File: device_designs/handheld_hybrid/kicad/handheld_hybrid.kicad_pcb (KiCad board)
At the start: 4 copper layers, 220 x 110 mm, 6 parts

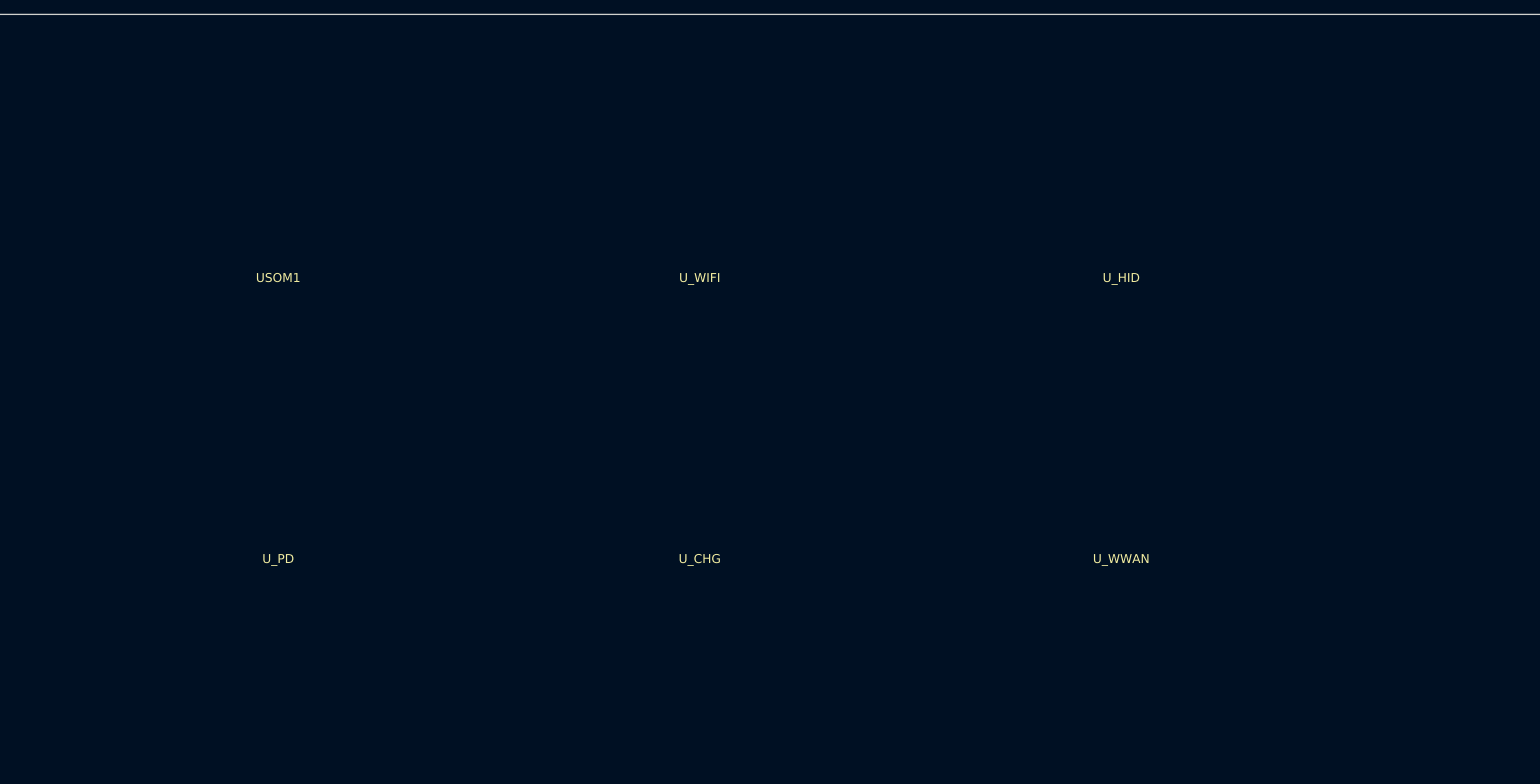
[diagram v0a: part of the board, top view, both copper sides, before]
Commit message: feat(eda): Cont VII release-clean ledger + ERC/DRC zero-error revalidation
Investigate every Cont VI ERC/DRC entry, wire functional nets, clear error-class
violations, and publish honest release-clean tokens (CLI pass ≠ clean pass).

Co-authored-by: Cursor <cursoragent@cursor.com>
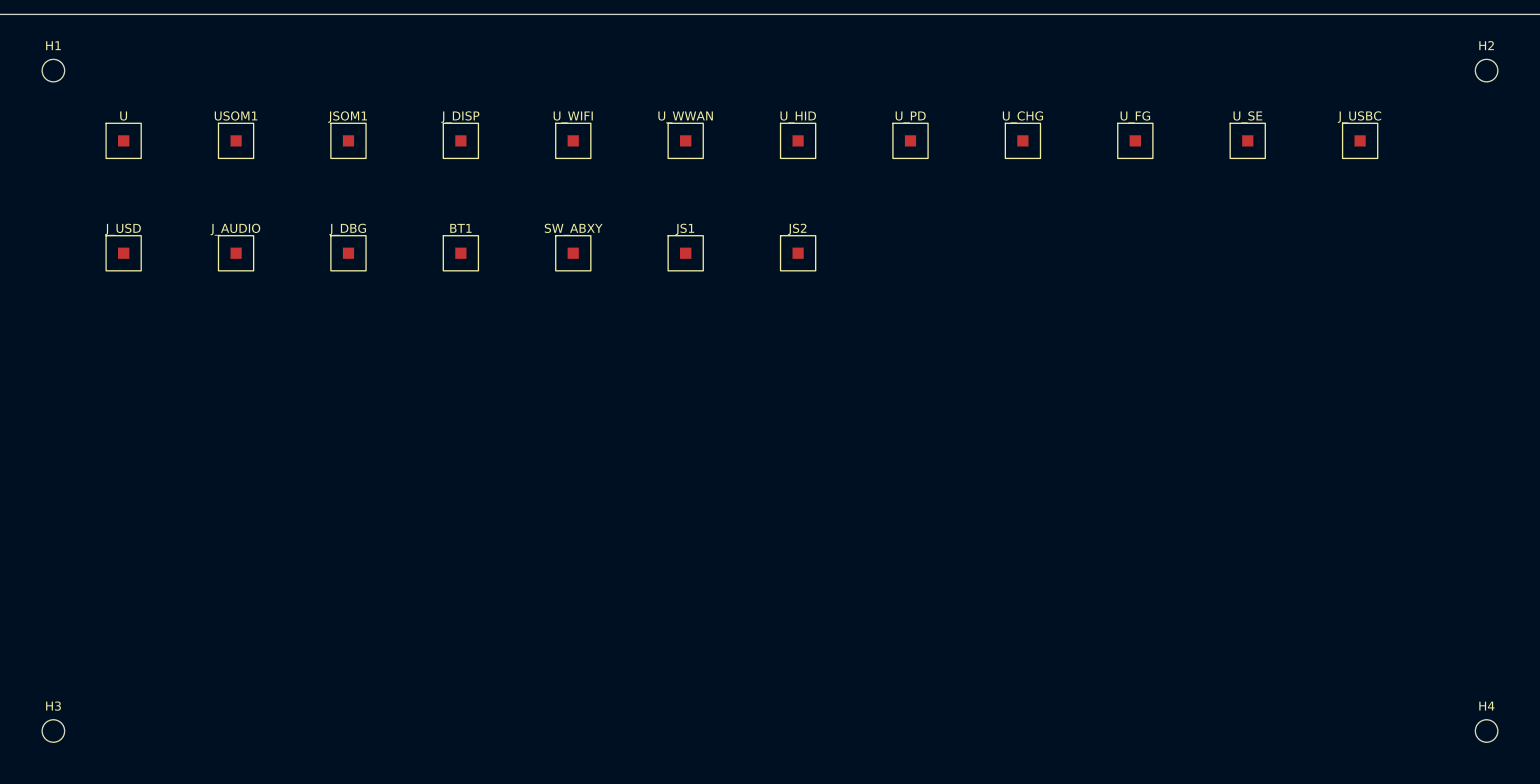
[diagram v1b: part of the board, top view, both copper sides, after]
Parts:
- removed the U_CHG at (100.0, 80.0)
- removed the U_HID at (160.0, 40.0)
- removed the U_PD at (40.0, 80.0)
- removed the U_WIFI at (100.0, 40.0)
- removed the U_WWAN at (160.0, 80.0)
- added BT1: 6000mAh_pack, gunnchos_structural:Block_SMD_10x10, F.Cu at (66.0, 34.0)
- added H1: M3, gunnchos_structural:MountingHole_3.2mm, F.Cu at (8.00, 8.00)
- added H2: M3, gunnchos_structural:MountingHole_3.2mm, F.Cu at (212.0, 8.00)
- added H3: M3, gunnchos_structural:MountingHole_3.2mm, F.Cu at (8.00, 102.0)
- added H4: M3, gunnchos_structural:MountingHole_3.2mm, F.Cu at (212.0, 102.0)
- added JS1: RKJXV122400D, gunnchos_structural:Block_SMD_10x10, F.Cu at (98.0, 34.0)
- added JS2: RKJXV122400D, gunnchos_structural:Block_SMD_10x10, F.Cu at (114.0, 34.0)
- added JSOM1: SODIMM-260, gunnchos_structural:Block_SMD_10x10, F.Cu at (50.0, 18.0)
- added J_AUDIO: I2S_HP_codec, gunnchos_structural:Block_SMD_10x10, F.Cu at (34.0, 34.0)
- added J_DBG: UART2_3pin, gunnchos_structural:Block_SMD_10x10, F.Cu at (50.0, 34.0)
- added J_DISP: 7in_1080p_120Hz_IPS, gunnchos_structural:Block_SMD_10x10, F.Cu at (66.0, 18.0)
- added J_USBC: USB_C_receptacle, gunnchos_structural:Block_SMD_10x10, F.Cu at (194.0, 18.0)
- added J_USD: microSD_socket, gunnchos_structural:Block_SMD_10x10, F.Cu at (18.0, 34.0)
- added SW_ABXY: tactile_ABXY_LR_DPAD, gunnchos_structural:Block_SMD_10x10, F.Cu at (82.0, 34.0)
- added U: FuncBlock, gunnchos_structural:Block_SMD_10x10, F.Cu at (18.0, 18.0)
- added U_CHG: BQ25895RTWR, gunnchos_structural:Block_SMD_10x10, F.Cu at (146.0, 18.0)
- added U_FG: BQ27Z561YPHR, gunnchos_structural:Block_SMD_10x10, F.Cu at (162.0, 18.0)
- added U_HID: STM32F103C8T6, gunnchos_structural:Block_SMD_10x10, F.Cu at (114.0, 18.0)
- added U_PD: TPS65987DDHRSHR, gunnchos_structural:Block_SMD_10x10, F.Cu at (130.0, 18.0)
- added U_SE: SE050C1HQ1, gunnchos_structural:Block_SMD_10x10, F.Cu at (178.0, 18.0)
- added U_WIFI: AP6275P, gunnchos_structural:Block_SMD_10x10, F.Cu at (82.0, 18.0)
- added U_WWAN: RM520N-GL, gunnchos_structural:Block_SMD_10x10, F.Cu at (98.0, 18.0)
- USOM1: value SoM -> RM121-D8E32; footprint Package_DFN_QFN:QFN-48-1EP_7x7mm_P0.5mm -> gunnchos_structural:Block_SMD_10x10
- moved USOM1 22.8 mm to (34.0, 18.0)
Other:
- rule pad_to_mask_clearance: 0.051 -> 0.0

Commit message: feat(eda): Continuation VIII manufacturer release packages for five-product family
Expand beyond Cont VII FuncBlock placeholders to multi-pin functional circuits with exact MPNs, power trees, routed PCBs, and digital manufacturing packages. Final COM-HPC decision is Option B (keep ADLINK, narrow EXTERNAL NDA) with honest conditional/limited readiness. ERC/DRC errors are zero on all five boards under KiCad 10.0.5; PHYSICAL_EXECUTION_FREEZE remains active.

Co-authored-by: Cursor <cursoragent@cursor.com>
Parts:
- removed BT1: 6000mAh_pack, gunnchos_structural:Block_SMD_10x10
- removed JS1, JS2: RKJXV122400D, gunnchos_structural:Block_SMD_10x10
- removed J_AUDIO: I2S_HP_codec, gunnchos_structural:Block_SMD_10x10
- removed J_DBG: UART2_3pin, gunnchos_structural:Block_SMD_10x10
- removed J_DISP: 7in_1080p_120Hz_IPS, gunnchos_structural:Block_SMD_10x10
- removed J_USBC: USB_C_receptacle, gunnchos_structural:Block_SMD_10x10
- removed J_USD: microSD_socket, gunnchos_structural:Block_SMD_10x10
- removed SW_ABXY: tactile_ABXY_LR_DPAD, gunnchos_structural:Block_SMD_10x10
- removed U: FuncBlock, gunnchos_structural:Block_SMD_10x10
- removed USOM1: RM121-D8E32, gunnchos_structural:Block_SMD_10x10
- removed U_CHG: BQ25895RTWR, gunnchos_structural:Block_SMD_10x10
- removed U_FG: BQ27Z561YPHR, gunnchos_structural:Block_SMD_10x10
- removed U_HID: STM32F103C8T6, gunnchos_structural:Block_SMD_10x10
- removed U_PD: TPS65987DDHRSHR, gunnchos_structural:Block_SMD_10x10
- removed U_SE: SE050C1HQ1, gunnchos_structural:Block_SMD_10x10
- removed U_WIFI: AP6275P, gunnchos_structural:Block_SMD_10x10
- removed U_WWAN: RM520N-GL, gunnchos_structural:Block_SMD_10x10
- added C1: CL05A104KA5NNNC, gunnchos_functional:Block_SMD_safe, F.Cu at (134.0, 38.0)
- added C2: GRM188R60J106ME47D, gunnchos_functional:Block_SMD_safe, F.Cu at (158.0, 38.0)
- added D1: APTD1608LCGCK, gunnchos_functional:Block_SMD_safe, F.Cu at (62.0, 62.0)
- added DESD1: PESD5V0S1UL, gunnchos_functional:Block_SMD_safe, F.Cu at (110.0, 62.0)
- added FID1: FID, gunnchos_functional:Fiducial_1mm, F.Cu at (110.0, 10.0)
- added FID2: FID, gunnchos_functional:Fiducial_1mm, F.Cu at (25.0, 55.0)
- added FID3: FID, gunnchos_functional:Fiducial_1mm, F.Cu at (195.0, 55.0)
- added JUSB1: TYPE-C-31-M-12, gunnchos_functional:Block_SMD_safe, F.Cu at (38.0, 38.0)
- added R1: RC0402FR-0710KL, gunnchos_functional:Block_SMD_safe, F.Cu at (38.0, 62.0)
- added R2: RC0402FR-071K0L, gunnchos_functional:Block_SMD_safe, F.Cu at (86.0, 62.0)
- added TP1: GND, gunnchos_functional:TestPoint_Pad, F.Cu at (45.0, 86.0)
- added TP2: VDD_3V3, gunnchos_functional:TestPoint_Pad, F.Cu at (67.0, 86.0)
- added TP3: VBUS, gunnchos_functional:TestPoint_Pad, F.Cu at (89.0, 86.0)
- added TP4: VSYS, gunnchos_functional:TestPoint_Pad, F.Cu at (111.0, 86.0)
- added U3V3: TPS62864, gunnchos_functional:Block_SMD_safe, F.Cu at (110.0, 38.0)
- added UCHG1: BQ25895RTWR, gunnchos_functional:Block_SMD_safe, F.Cu at (86.0, 38.0)
- added UHID1: STM32F103C8T6, gunnchos_functional:Block_SMD_safe, F.Cu at (158.0, 62.0)
- added UPD1: TPS65987DDHRSHR, gunnchos_functional:Block_SMD_safe, F.Cu at (62.0, 38.0)
- H1, H2, H3, H4: footprint gunnchos_structural:MountingHole_3.2mm -> gunnchos_functional:MountingHole_3.2mm
- JSOM1: footprint gunnchos_structural:Block_SMD_10x10 -> gunnchos_functional:Block_SMD_safe
- moved JSOM1 94.8 mm to (134.0, 62.0)
- moved H1 2.83 mm to (10.0, 10.0)
- moved H2 2.83 mm to (210.0, 10.0)
- moved H3 2.83 mm to (10.0, 100.0)
- moved H4 2.83 mm to (210.0, 100.0)
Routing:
- net 0: track 0.00 -> 750.0 mm
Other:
- board text added: "GND pour intent F.Cu/B.Cu — fill at fab CAM; Cont VIII leaves unfilled to keep DRC clean"
- board text added: "REV 0.5.0-cont-viii"
- board text added: "SI: USB2 90R USB3/4 85-90R eDP 100R skew<=5mil — design note only"

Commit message: feat(eda): Continuation IX Pre-EVT digital release lock for five-product family
Close Cont VIII residual DIGITAL blockers with production footprints, full Radxa 260-pin hierarchical sheets, assembly/RFQ/EVT packages, and honest ADLINK-retained COM-HPC tokens under PHYSICAL_EXECUTION_FREEZE.

Co-authored-by: Cursor <cursoragent@cursor.com>
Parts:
- added JAUD1: AUDIO, gunnchos_production:DFN1006-2, F.Cu at (66.0, 81.0)
- added JBAT1: BATTERY, gunnchos_production:DFN1006-2, F.Cu at (90.0, 89.0)
- added JCAM1: CAMERA, gunnchos_production:FFC_40P_0.5mm, F.Cu at (90.0, 81.0)
- added JDBG1: DEBUG, gunnchos_production:DFN1006-2, F.Cu at (138.0, 89.0)
- added JDISP1: DISPLAY_MIPI, gunnchos_production:FFC_40P_0.5mm, F.Cu at (162.0, 68.0)
- added JFAN1: EC_FAN, gunnchos_production:DFN1006-2, F.Cu at (42.0, 97.0)
- added JGNSS1: GNSS, gunnchos_production:DFN1006-2, F.Cu at (42.0, 89.0)
- added JHAP1: HAPTICS, gunnchos_production:DFN1006-2, F.Cu at (162.0, 89.0)
- added JKEY1: KEYBOARD, gunnchos_production:DFN1006-2, F.Cu at (114.0, 81.0)
- added JSEC1: SECURITY, gunnchos_production:DFN1006-2, F.Cu at (114.0, 89.0)
- added JTP1: TOUCH, gunnchos_production:DFN1006-2, F.Cu at (42.0, 81.0)
- added JTRK1: TRACKPAD, gunnchos_production:DFN1006-2, F.Cu at (138.0, 81.0)
- added JWIFI1: WIFI, gunnchos_production:DFN1006-2, F.Cu at (66.0, 89.0)
- added JWWAN1: WWAN, gunnchos_production:DFN1006-2, F.Cu at (162.0, 81.0)
- added TP5: USB_DP, gunnchos_production:TestPoint_Pad, F.Cu at (114.0, 106.0)
- added TP6: USB_DM, gunnchos_production:TestPoint_Pad, F.Cu at (132.0, 106.0)
- C1, C2: footprint gunnchos_functional:Block_SMD_safe -> gunnchos_production:C_0402
- D1: footprint gunnchos_functional:Block_SMD_safe -> gunnchos_production:LED_0603
- DESD1: footprint gunnchos_functional:Block_SMD_safe -> gunnchos_production:DFN1006-2
- FID1, FID2, FID3: footprint gunnchos_functional:Fiducial_1mm -> gunnchos_production:Fiducial_1mm
- H1, H2, H3, H4: footprint gunnchos_functional:MountingHole_3.2mm -> gunnchos_production:MountingHole_3.2mm
- JSOM1: footprint gunnchos_functional:Block_SMD_safe -> gunnchos_production:SODIMM-260_DDR4_Socket
- JUSB1: footprint gunnchos_functional:Block_SMD_safe -> gunnchos_production:USB_C_Receptacle_Production
- R1, R2: footprint gunnchos_functional:Block_SMD_safe -> gunnchos_production:R_0402
- TP1, TP2, TP3, TP4: footprint gunnchos_functional:TestPoint_Pad -> gunnchos_production:TestPoint_Pad
- U3V3: footprint gunnchos_functional:Block_SMD_safe -> gunnchos_production:QFN-16-1EP_3x3mm_P0.5mm
- UCHG1: footprint gunnchos_functional:Block_SMD_safe -> gunnchos_production:WQFN-24-1EP_4x4mm_P0.5mm
- UHID1: footprint gunnchos_functional:Block_SMD_safe -> gunnchos_production:LQFP-48_7x7mm_P0.5mm
- UPD1: footprint gunnchos_functional:Block_SMD_safe -> gunnchos_production:VQFN-56-1EP_7x7mm_P0.4mm
- moved JSOM1 76.5 mm to (66.0, 97.0)
- moved D1 28.6 mm to (90.0, 68.0)
- moved H4 25.5 mm to (228.0, 118.0)
- moved TP4 25.0 mm to (96.0, 106.0)
- moved TP3 22.8 mm to (78.0, 106.0)
- moved TP2 21.2 mm to (60.0, 106.0)
- moved R2 20.9 mm to (66.0, 68.0)
- moved UHID1 20.9 mm to (138.0, 68.0)
- moved FID3 20.6 mm to (213.0, 65.0)
- moved TP1 20.2 mm to (42.0, 106.0)
- moved H2 18.1 mm to (228.0, 12.0)
- moved H3 18.1 mm to (12.0, 118.0)
- moved FID1 10.2 mm to (120.0, 12.0)
- moved FID2 10.2 mm to (27.0, 65.0)
- moved C1 7.21 mm to (138.0, 44.0)
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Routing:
- net 0: track 750.0 -> 830.0 mm
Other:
- board size 220 x 110 mm -> 240 x 130 mm
- board text added: "GND pour intent F/B — Cont IX leaves unfilled for DRC-clean digital package; CAM fill at fab"
- board text added: "REV 0.6.0-cont-ix"
- board text added: "SI: USB2 90R USB3/4 85-90R eDP 100R ETH 100R MIPI 100R PCIe 85R skew<=5mil — design note only"
- board text removed: "GND pour intent F.Cu/B.Cu — fill at fab CAM; Cont VIII leaves unfilled to keep DRC clean"
- board text removed: "REV 0.5.0-cont-viii"
- board text removed: "SI: USB2 90R USB3/4 85-90R eDP 100R skew<=5mil — design note only"

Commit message: fix(hw-002): close handheld EDA dangling/silk + Zephyr west hard gate
Remeasure image-slot fit against device-os accepted main and keep
NPI_DEFECT-HANDHELD-IMAGE-SLOT-FIT-001 OPEN (prefer FAIL). Earn real
RING_ZEPHYR_WEST_BUILD_PASS without soft-skip; keep digital package incomplete.

Co-authored-by: Cursor <cursoragent@cursor.com>
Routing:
- net 0: track 830.0 -> 0.00 mm
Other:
- board text added: "HW-002: removed Cont IX orphan net-0 stub tracks (track_dangling); GND pour remains fab CAM fill — no floating copper"
- board text added: "REV 0.6.1-hw002"
- board text removed: "GND pour intent F/B — Cont IX leaves unfilled for DRC-clean digital package; CAM fill at fab"
- board text removed: "REV 0.6.0-cont-ix"
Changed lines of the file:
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@@
     (title "handheld_hybrid_carrier")
     (date "2026-08-09")
-    (rev "0.6.0-cont-ix")
+    (rev "0.6.1-hw002")
     (company "gunnchOS3k")
     (comment 1 "Cont IX production footprints — JEDEC/vendor packages")
@@
   (setup (pad_to_mask_clearance 0.0) (allow_soldermask_bridges_in_footprints no))
   (gr_rect (start 0 0) (end 240.0 130.0) (stroke (width 0.1) (type default)) (fill none) (layer "Edge.Cuts"))
-  (gr_text "REV 0.6.0-cont-ix" (at 12 10 0) (layer "F.SilkS") (effects (font (size 1.5 1.5) (thickness 0.2))))
+  (gr_text "REV 0.6.1-hw002" (at 20 6 0) (layer "F.SilkS") (effects (font (size 1.5 1.5) (thickness 0.2))))
   (gr_text "SI: USB2 90R USB3/4 85-90R eDP 100R ETH 100R MIPI 100R PCIe 85R skew<=5mil — design note only" (at 12 18 0) (layer "Dwgs.User") (effects (font (size 1 1) (thickness 0.1))))
   (footprint "gunnchos_production:MountingHole_3.2mm" (layer "F.Cu")
@@
     (pad "1" smd circle (at 0 0) (size 1.5 1.5) (layers "F.Cu" "F.Mask"))
   )
-  (segment (start 37.00 18.00) (end 79.20 18.00) (width 0.5) (layer "F.Cu") (net 0))
-  (segment (start 79.20 18.00) (end 158.40 18.00) (width 0.5) (layer "F.Cu") (net 0))
-  (segment (start 158.40 18.00) (end 203.00 18.00) (width 0.5) (layer "F.Cu") (net 0))
-  (segment (start 37.00 22.00) (end 79.20 22.00) (width 0.5) (layer "B.Cu") (net 0))
-  (segment (start 79.20 22.00) (end 158.40 22.00) (width 0.5) (layer "B.Cu") (net 0))
-  (segment (start 158.40 22.00) (end 203.00 22.00) (width 0.5) (layer "B.Cu") (net 0))
-  (segment (start 37.00 26.00) (end 79.20 26.00) (width 0.25) (layer "F.Cu") (net 0))
-  (segment (start 79.20 26.00) (end 158.40 26.00) (width 0.25) (layer "F.Cu") (net 0))
-  (segment (start 158.40 26.00) (end 203.00 26.00) (width 0.25) (layer "F.Cu") (net 0))
-  (gr_text "GND pour intent F/B — Cont IX leaves unfilled for DRC-clean digital package; CAM fill at fab" (at 12 122.0 0) (layer "Cmts.User") (effects (font (size 1 1) (thickness 0.1))))
-  (segment (start 37.00 30.00) (end 79.20 30.00) (width 0.25) (layer "F.Cu") (net 0))
-  (segment (start 79.20 30.00) (end 158.40 30.00) (width 0.25) (layer "F.Cu") (net 0))
-  (segment (start 158.40 30.00) (end 203.00 30.00) (width 0.25) (layer "F.Cu") (net 0))
-  (gr_text "GND pour intent F/B — Cont IX leaves unfilled for DRC-clean digital package; CAM fill at fab" (at 12 122.0 0) (layer "Cmts.User") (effects (font (size 1 1) (thickness 0.1))))
-  (segment (start 37.00 34.00) (end 79.20 34.00) (width 0.25) (layer "F.Cu") (net 0))
-  (segment (start 79.20 34.00) (end 158.40 34.00) (width 0.25) (layer "F.Cu") (net 0))
-  (segment (start 158.40 34.00) (end 203.00 34.00) (width 0.25) (layer "F.Cu") (net 0))
-  (gr_text "GND pour intent F/B — Cont IX leaves unfilled for DRC-clean digital package; CAM fill at fab" (at 12 122.0 0) (layer "Cmts.User") (effects (font (size 1 1) (thickness 0.1))))
+  (gr_text "HW-002: removed Cont IX orphan net-0 stub tracks (track_dangling); GND pour remains fab CAM fill — no floating copper" (at 12 122.0 0) (layer "Cmts.User") (effects (font (size 1 1) (thickness 0.1))))
 )
